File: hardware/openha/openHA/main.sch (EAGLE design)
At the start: 65 parts, among them J1 HP_Con, J3 Bat_Con, U10 STBC08, U11 STM32L476JX, U2 MP34DT05-A, U3 MP34DT05-A, U4 PCM1774RGPR, U5 BLUENRG-MS, U6 LD39115J, U7 STC3115IQT, U8 USBLC6-2, U9 LD39115J, Y1 32.768kHz

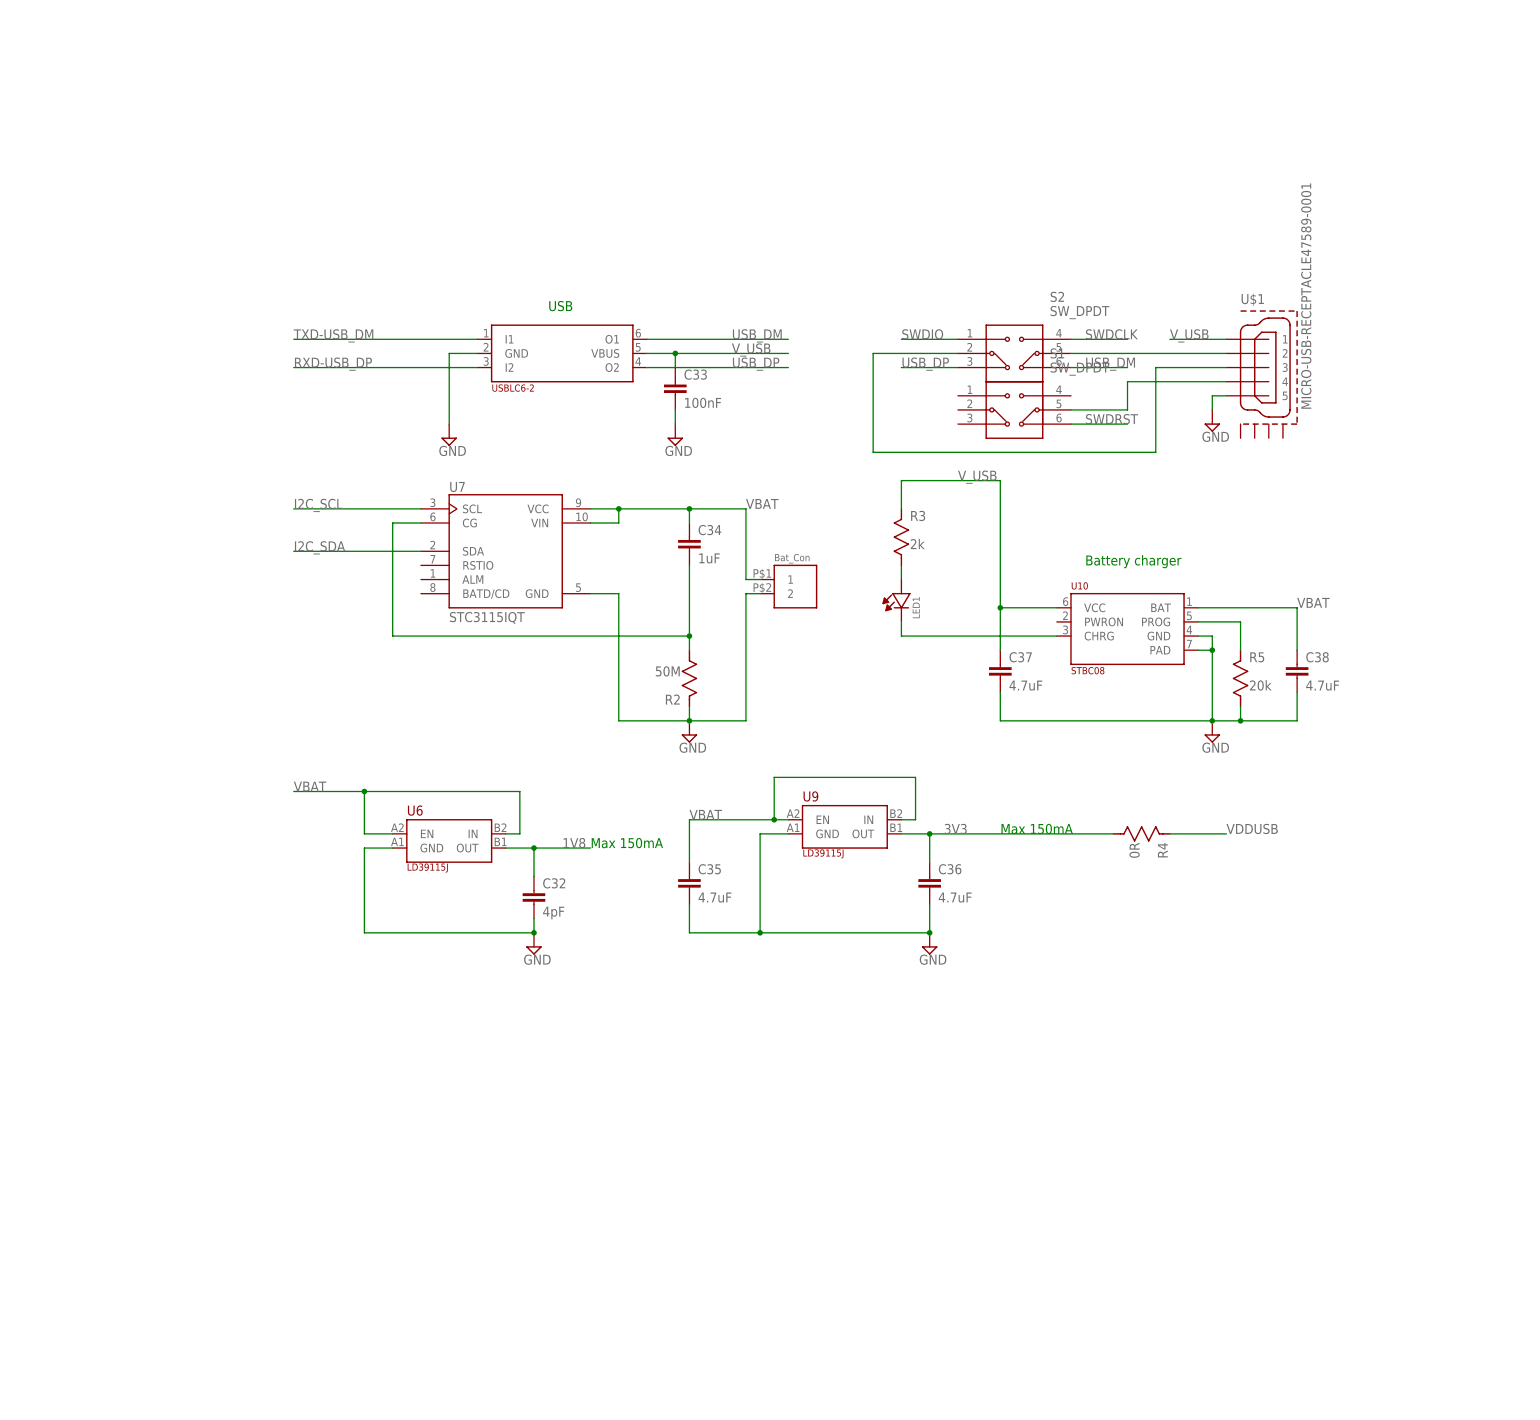
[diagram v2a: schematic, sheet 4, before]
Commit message: WIP-BOM Update
Update BOM for battery charger and gauge
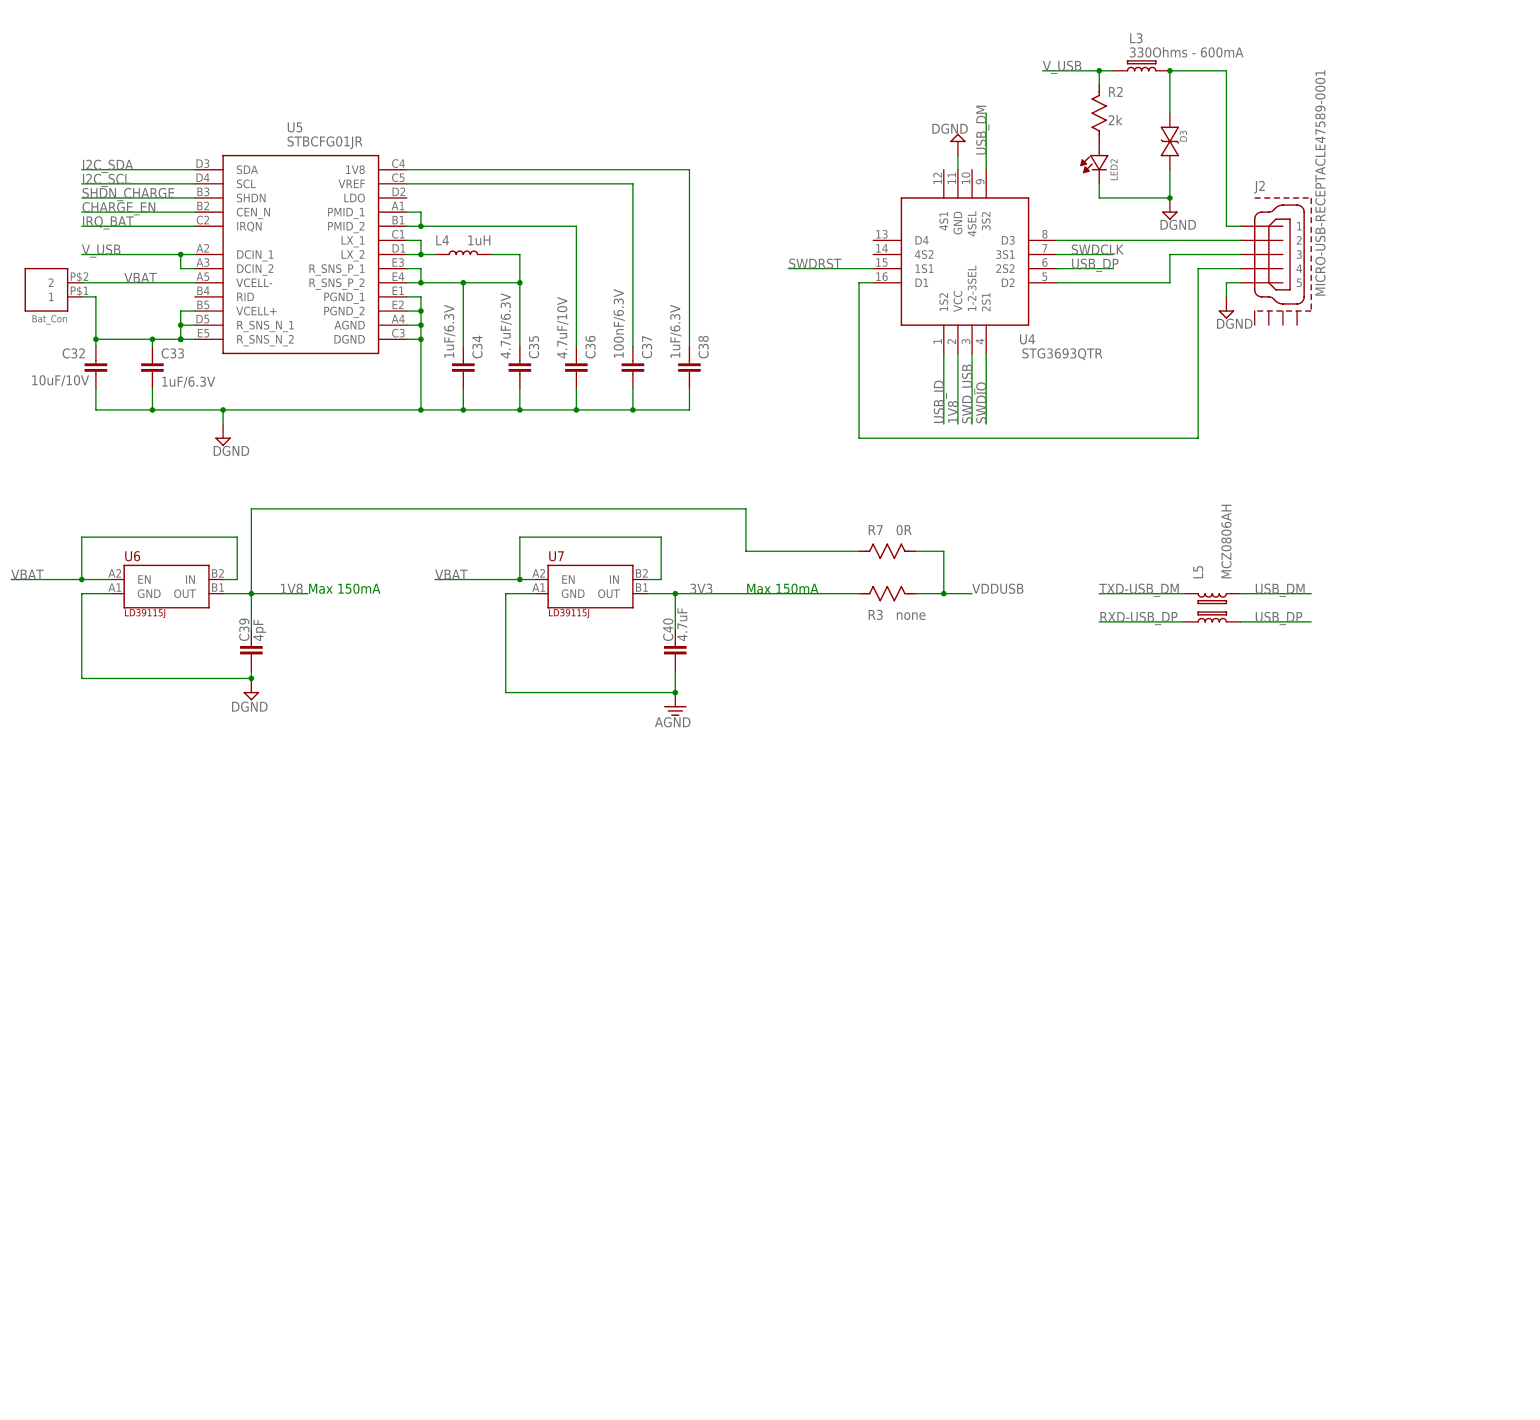
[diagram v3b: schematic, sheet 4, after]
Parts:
- removed S1, S2: SW_DPDT, OAlib:SW_DPDT
- removed U$1: MICRO-USB-RECEPTACLE47589-0001, OAlib:MICRO-USB-RECEPTACLE47589-0001
- removed U10: STBC08, OAlib:STBC08
- removed U8: USBLC6-2, OAlib:USBLC6-2
- removed U9: LD39115J, OAlib:LD39115J
- added C39: 4pF, OAlib:C_NP0603
- added C40: 4.7uF, OAlib:C_NP0603
- added D1, D2, D3: (no value), OAlib:TVS_DIODE_B
- added J2: MICRO-USB-RECEPTACLE47589-0001, OAlib:MICRO-USB-RECEPTACLE47589-0001
- added L2: BALF-NRG-01D3, OAlib:BALF-NRG-01D3
- added L4: 1uH, OAlib:L
- added L5: MCZ0806AH, OAlib:MCZ0806AH
- added MIC1, MIC2: MP34DT05-A, OAlib:MP34DT05-A
- added R6: 4.7k, OAlib:R
- added R7: 0R, OAlib:R
- C1, C10, C11, C12, C14, C16, C17, C18, C19, C25, C4, C5, C6, C8, C9: device OAlib:CAP0603 -> OAlib:C_NP0603
- C13: value 100nF -> 4.7uF; device OAlib:CAP0603 -> OAlib:C_NP0603
- C15: value 4.7uF -> 100nF; device OAlib:CAP0603 -> OAlib:C_NP0603
- C2: value 1uF -> 4pF; device OAlib:CAP0603 -> OAlib:C_NP0603
- C20: value 100pF -> 15pF; device OAlib:CAP0603 -> OAlib:C_NP0603
- C21: value 100nF -> 15pF; device OAlib:CAP0603 -> OAlib:C_NP0603
- C22: value 2.2uF -> 100nF; device OAlib:CAP0603 -> OAlib:C_NP0603
- C23, C7: value 100nF -> 1uF; device OAlib:CAP0603 -> OAlib:C_NP0603
- C24: value 2.2uF -> 100pF; device OAlib:CAP0603 -> OAlib:C_NP0603
- C26: value 15pF -> 2.2uF; device OAlib:CAP0603 -> OAlib:C_NP0603
- C27: value 150nF -> 100nF; device OAlib:CAP0603 -> OAlib:C_NP0603
- C28: value 100p -> 2.2uF; device OAlib:CAP0603 -> OAlib:C_NP0603
- C29: value 15pF -> 100nF; device OAlib:CAP0603 -> OAlib:C_NP0603
- C3: value 4pF -> 100nF; device OAlib:CAP0603 -> OAlib:C_NP0603
- C30: value 100nF -> 150nF; device OAlib:CAP0603 -> OAlib:C_NP0603
- C31: value 1uF -> 100p; device OAlib:CAP0603 -> OAlib:C_NP0603
- C32: value 4pF -> 10uF/10V; device OAlib:CAP0603 -> OAlib:C_NP0603
- C33: value 100nF -> 1uF/6.3V; device OAlib:CAP0603 -> OAlib:C_NP0603
- C34: value 1uF -> 1uF/6.3V; device OAlib:CAP0603 -> OAlib:C_NP0603
- C35: value 4.7uF -> 4.7uF/6.3V; device OAlib:CAP0603 -> OAlib:C_NP0603
- C36: value 4.7uF -> 4.7uF/10V; device OAlib:CAP0603 -> OAlib:C_NP0603
- C37: value 4.7uF -> 100nF/6.3V; device OAlib:CAP0603 -> OAlib:C_NP0603
- C38: value 4.7uF -> 1uF/6.3V; device OAlib:CAP0603 -> OAlib:C_NP0603
- L1: value BALF-NRG-01D3 -> 3.9nH; device OAlib:BALF-NRG-01D3 -> OAlib:L
- L3: value 3.9nH -> 330Ohms - 600mA; device OAlib:L -> OAlib:L_EMI0402
- R1: device OAlib:RESISTOR -> OAlib:R
- R2: value 50M -> 2k; device OAlib:RESISTOR -> OAlib:R
- R3: value 2k -> none; device OAlib:RESISTOR -> OAlib:R
- R4: value 0R -> 4.7k; device OAlib:RESISTOR -> OAlib:R
- R5: value 20k -> 4.7k; device OAlib:RESISTOR -> OAlib:R
- U2: value MP34DT05-A -> PCM1774RGPR; device OAlib:MP34DT05-A -> PCM1774:PCM1774RGPR
- U3: value MP34DT05-A -> BLUENRG-MS; device OAlib:MP34DT05-A -> OAlib:BLUENRG-MS
- U4: value PCM1774RGPR -> STG3693QTR; device PCM1774:PCM1774RGPR -> OAlib:STG3693QTR
- U5: value BLUENRG-MS -> STBCFG01JR; device OAlib:BLUENRG-MS -> OAlib:STBCFG01JR
- U7: value STC3115IQT -> LD39115J; device STC3115IQT:STC3115IQT -> OAlib:LD39115J
- renumbered U$2 to X2, U11 to U1, Y1 to X1
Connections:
- removed net CHRG: LED1.K, U10.CHRG
- removed net GND: A1.P$2, C1.2, C10.2, C11.2, C12.2, C13.1, C14.1, C15.1, C16.1, C17.1, C2.2, C20.2, C21.2, C22.2, C23.2, C24.2, C25.2, C26.2, C27.2, C28.2, C3.2, C32.2, C33.2, C35.2, C36.2, C37.2, C38.2, C4.2, C5.2, C6.2, C7.2, C8.2, C9.2, J3.2, L1.GND, L3.2, LED2.K, R2.1, R5.2, U$1.5, U1.BOOT0, U1.VSS, U1.VSSA/VREF-, U1.VSS_2, U1.VSS_3, U1.VSS_4, U10.GND, U10.PAD, U2.GND, U2.LR, U3.GND, U3.LR, U4.AGND, U4.DGND, U4.EPAD, U4.MS/ADR, U4.PGND, U5.GND_1, U5.GND_2, U5.GND_3, U5.SMPS-GND, U5.TEST10, U5.TEST11, U5.TEST12, U5.TEST2, U5.TEST3, U5.TEST4, U5.TEST5, U5.TEST6, U5.TEST7, U5.TEST8, U5.TEST9, U6.GND, U7.GND, U8.GND, U9.GND, X2.P$2, X2.P$4
- removed net N$20: U1.PA10
- removed net N$8: R5.1, U10.PROG
- new net AGND: C17.1, C18.1, C19.1, C40.2, D1.K, D2.K, U2.AGND, U2.PGND, U7.GND
- new net CHARGE_EN: U1.PB15, U5.CEN_N
- new net DGND: A1.P$2, C1.2, C10.2, C11.2, C12.2, C15.1, C16.1, C2.2, C20.2, C24.2, C25.2, C26.2, C27.2, C28.2, C29.2, C3.2, C30.2, C31.2, C32.2, C33.2, C34.2, C35.2, C36.2, C37.2, C38.2, C39.2, C4.2, C5.2, C6.2, C7.2, C8.2, C9.2, D3.K, J2.5, L1.2, L2.GND, LED1.K, LED2.K, MIC1.GND, MIC1.LR, MIC2.GND, MIC2.LR, U1.BOOT0, U1.VSS, U1.VSSA/VREF-, U1.VSS_2, U1.VSS_3, U1.VSS_4, U2.DGND, U2.MS/ADR, U3.GND_1, U3.GND_2, U3.GND_3, U3.SMPS-GND, U3.TEST10, U3.TEST11, U3.TEST12, U3.TEST2, U3.TEST3, U3.TEST4, U3.TEST5, U3.TEST6, U3.TEST7, U3.TEST8, U3.TEST9, U4.GND, U5.AGND, U5.DGND, U5.PGND_1, U5.PGND_2, U6.GND, X2.P$2, X2.P$4
- new net IRQ_BAT: U1.PC7, U5.IRQN
- new net N$18: C38.1, U5.1V8
- new net N$21: C36.1, U5.PMID_1, U5.PMID_2
- new net N$22: C34.1, C35.1, L4.2, U5.R_SNS_P_1, U5.R_SNS_P_2
- new net N$25: L4.1, U5.LX_1, U5.LX_2
- new net N$27: C32.1, C33.1, J3.1, U5.R_SNS_N_1, U5.R_SNS_N_2, U5.VCELL+
- new net SHDN_CHARGE: U1.PB12, U5.SHDN
- new net SWD_USB: R6.2, U1.PC9, U4.1-2-3SEL
- new net USB_ID: U1.PA10, U4.1S2
- net 1V8: now also C15.2, C16.2, C22.2, C23.2, C26.1, C29.1, C3.1, C30.1, C31.1, C39.1, MIC1.VDD, MIC2.VDD, R4.1, R5.1, R6.1, R7.2, U1.VDDIO2, U2.MODE, U2.VIO, U3.VBAT1, U3.VBAT3, U3.VDD1V2, U3.VDD1V8, U4.VCC; no longer C2.1, C20.1, C21.1, C22.1, C23.1, C30.2, C31.2, C32.1, U3.VDD, U5.VBAT1, U5.VBAT3, U5.VDD1V2, U5.VDD1V8
- net 3V3: now also C18.2, C19.2, C40.1, R3.2, U2.VCC, U2.VCOM, U2.VPA, U7.OUT; no longer C13.2, C14.2, C15.2, C16.2, C36.1, R4.2, U4.MODE, U4.VCC, U4.VCOM, U4.VDD, U4.VIO, U4.VPA, U9.OUT
- net BLUE_CLK: now also U3.SPI_CLK; no longer U5.SPI_CLK
- net BLUE_CS: now also U3.SPI_CS; no longer U5.SPI_CS
- net BLUE_IRQ: now also U3.SPI_IRQ; no longer U5.SPI_IRQ
- net BLUE_MISO: now also U3.SPI_MISO; no longer U5.SPI_MISO
- net BLUE_MOSI: now also U3.SPI_MOSI; no longer U5.SPI_MOSI
- net HPL: now also C13.2, D2.A; no longer C18.2
- net HPR: now also C14.2, D1.A; no longer C19.2
- net I2C_SCL: now also R4.2, U2.MC/SCL, U5.SCL; no longer U4.MC/SCL, U7.SCL
- net I2C_SDA: now also R5.2, U2.MD/SDA, U5.SDA; no longer U4.MD/SDA, U7.SDA
- net MIC1_CLK: now also MIC1.CLK; no longer U2.CLK
- net MIC1_DATA: now also MIC1.DOUT; no longer U2.DOUT
- net MIC2_CLK: now also MIC2.CLK; no longer U3.CLK
- net MIC2_DATA: now also MIC2.DOUT; no longer U3.DOUT
- net N$10: now also C14.1, U2.HPOR/LOR; no longer C19.1, U4.HPOR/LOR
- net N$11: now also J2.3, U4.D2; no longer S2.2, U$1.3
- net N$12: now also L2.ANT; no longer L1.ANT
- net N$13: now also L2.RX_P, U3.RF1; no longer L1.RX_P, U5.RF1
- net N$14: now also L2.RX_N, U3.RF0; no longer L1.RX_N, U5.RF0
- net N$15: now also LED1.A; no longer LED2.A
- net N$16: now also J2.4, U4.D1; no longer S1.5, U$1.4
- net N$19: now also C22.1, C23.1, U3.SMPSFILT2; no longer C30.1, C31.1, U5.SMPSFILT2
- net N$2: now also C21.2, L1.1; no longer C29.2, L3.1
- net N$3: now also C13.1, U2.HPOL/LOL; no longer C18.1, U4.HPOL/LOL
- net N$6: now also LED2.A, R2.2; no longer LED1.A, R3.2
- net N$7: now also C37.1, U5.VREF; no longer C34.2, R2.2, U7.CG
- net N$9: now also J2.2, U4.D3; no longer S2.5, U$1.2
- net OSC_BLUE_IN: now also C20.1, U3.FXTAL1; no longer C26.1, U5.FXTAL1
- net OSC_BLUE_OUT: now also C21.1, U3.FXTAL0; no longer C29.1, U5.FXTAL0
- net OSC_OUT: now also C2.1; no longer C3.1
- net RXD-USB_DP: now also L5.2; no longer U8.I2
- net SAI_BCK: now also U2.BCK; no longer U4.BCK
- net SAI_LR: now also U2.LRCK; no longer U4.LRCK
- net SAI_SCK: now also U2.SCKI; no longer U4.SCKI
- net SAI_SD: now also U2.DIN; no longer U4.DIN
- net SWDCLK: now also U4.3S1; no longer S2.4
- net SWDIO: now also U4.2S1; no longer S2.1
- net SWDRST: now also U4.1S1; no longer S1.6
- net TXD-USB_DM: now also L5.1; no longer U8.I1
- net USB_DM: now also L5.4, U4.3S2; no longer S2.6, U8.O1
- net USB_DP: now also L5.3, U4.2S2; no longer S2.3, U8.O2
- net VBAT: now also J3.2, U5.VCELL-, U7.EN, U7.IN; no longer C34.1, C35.1, C38.1, J3.1, U10.BAT, U7.VCC, U7.VIN, U9.EN, U9.IN
- net VDDUSB: now also R3.1, R7.1; no longer R4.1, U1.VDDIO2
- net V_USB: now also D3.A, J2.1, L3.1, L3.2, R2.1, U1.PA9, U5.DCIN_1, U5.DCIN_2; no longer C33.1, C37.1, R3.1, U$1.1, U10.VCC, U8.VBUS
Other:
- note removed: "Battery charger"
- note removed: "USB"
- moved on the sheet: C1, C10, C11, C12, C13, C14, C15, C16, C17, C18, C19, C2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

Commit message: WIP-BOM Update
Replace Bluetooth chips by a fully integrated module
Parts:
- removed A1: ANT, OAlib:ANT
- removed C21: 15pF, OAlib:C_NP0603
- removed C22, C25, C29: 100nF, OAlib:C_NP0603
- removed C23: 1uF, OAlib:C_NP0603
- removed C24: 100pF, OAlib:C_NP0603
- removed C28: 2.2uF, OAlib:C_NP0603
- removed C30: 150nF, OAlib:C_NP0603
- removed C31: 100p, OAlib:C_NP0603
- removed L1: 3.9nH, OAlib:L
- removed L2: BALF-NRG-01D3, OAlib:BALF-NRG-01D3
- removed U3: BLUENRG-MS, OAlib:BLUENRG-MS
- removed X2: 32MHz, OAlib:ABM11W-101
- added C41: 1pF, OAlib:C_NP0603
- added D4: 1.8V, OAlib:ZENERSOD-523
- added IC1: MBN52832, OAlib:MBN52832
- added L6: 1.1nH, OAlib:L
- added L7: 10nH, OAlib:L0402
- added L8: 10uH, OAlib:L0603
- added R10, R11: (no value), OAlib:R
- added R12: 10k, OAlib:R
- added R8: none, OAlib:R
- added R9: 4.7k, OAlib:R
- C20: value 15pF -> 4.7uF
- U6: REF (none) -> LD39115J18R
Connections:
- removed net N$12: A1.P$1, L2.ANT
- removed net N$13: L2.RX_P, U3.RF1
- removed net N$14: L2.RX_N, U3.RF0
- removed net N$19: C22.1, C23.1, U3.SMPSFILT2
- removed net OSC_BLUE_IN: C20.1, U3.FXTAL1, X2.P$1
- removed net OSC_BLUE_OUT: C21.1, U3.FXTAL0, X2.P$3
- removed net SWD_USB: R6.2, U1.PC9, U4.1-2-3SEL
- new net 4V85: R8.2, U5.LDO
- new net GND: C26.2, C27.2, C41.2, IC1.GND_1, IC1.GND_2, IC1.GND_3, IC1.GND_4, IC1.GND_5, IC1.GND_6, IC1.GND_7, IC1.GND_8
- new net N$20: C41.1, IC1.ANTOUT, L6.2
- new net N$23: C26.1, C27.1, IC1.VCC, R10.2, R11.2
- new net N$24: IC1.ANTIN, L6.1
- new net N$26: IC1.DCC, L7.2
- new net N$29: IC1.DEC, L8.1
- new net N$30: L7.1, L8.2
- new net SEL_STM_BLU: U4.4SEL
- new net SEL_SWD_USB: R6.2, R9.2, U1.PB1, U1.PC9, U4.1-2-3SEL
- new net SWDIO_BLU: IC1.SWDIO, U4.4S2
- new net SWDIO_STM: U1.PA13, U4.4S1
- net 1V8: now also R10.1, R9.1; no longer C22.2, C23.2, C24.1, C25.1, C26.1, C27.1, C28.1, C29.1, C30.1, C31.1, U1.VBAT, U3.VBAT1, U3.VBAT3, U3.VDD1V2, U3.VDD1V8, U4.VCC
- net 3V3: now also R11.1
- net BLUE_CLK: now also IC1.P0_06; no longer U3.SPI_CLK
- net BLUE_CS: now also IC1.P0_00/XL1; no longer U3.SPI_CS
- net BLUE_IRQ: now also IC1.P0_01/XL2; no longer U3.SPI_IRQ
- net BLUE_MISO: now also IC1.P0_07; no longer U3.SPI_MISO
- net BLUE_MOSI: now also IC1.P0_08; no longer U3.SPI_MOSI
- net DGND: now also D4.ANODE, J2.GND1, J2.GND2, J2.GND3, J2.GND4; no longer A1.P$2, C24.2, C25.2, C26.2, C27.2, C28.2, C29.2, C30.2, C31.2, L1.2, L2.GND, U3.GND_1, U3.GND_2, U3.GND_3, U3.SMPS-GND, U3.TEST10, U3.TEST11, U3.TEST12, U3.TEST2, U3.TEST3, U3.TEST4, U3.TEST5, U3.TEST6, U3.TEST7, U3.TEST8, U3.TEST9, X2.P$2, X2.P$4
- net N$2: now also C20.1, D4.CATHODE, R12.2, U1.VBAT; no longer C21.2, L1.1
- net SWDCLK: now also IC1.SWDCLK
- net SWDIO: now also U4.D4; no longer U1.PA13
- net SWDRST: now also IC1.P0_21/RESET
- net VBAT: now also R12.1
- net VDDUSB: now also R8.1, U4.VCC
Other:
- note removed: "Bluetooth"
- note removed: "Oscillator (BLUE)"
